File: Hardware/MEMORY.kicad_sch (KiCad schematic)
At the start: 11 parts, among them U20 AT24C256C

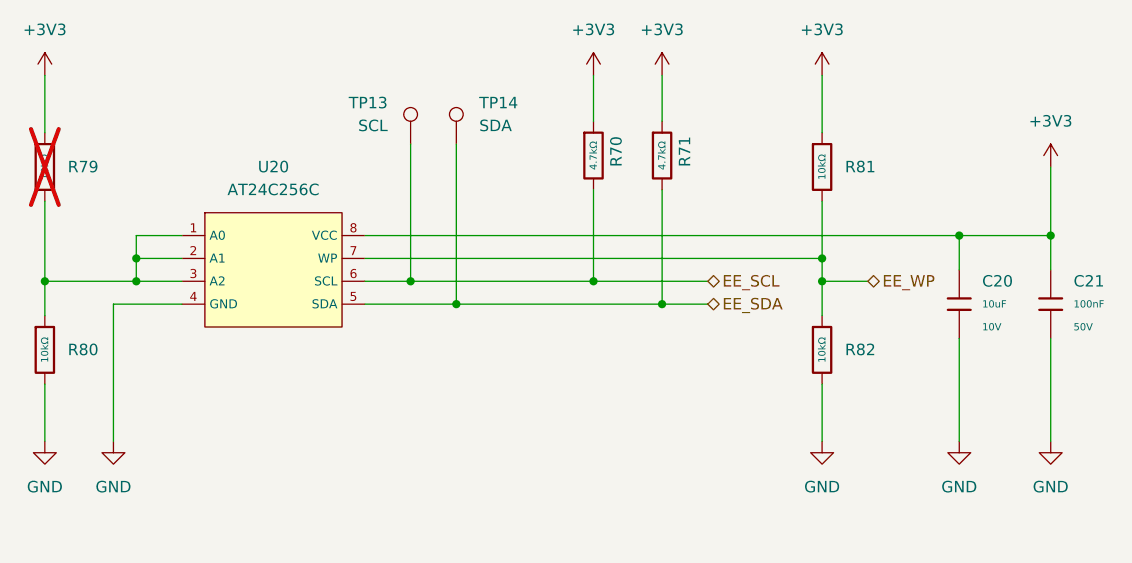
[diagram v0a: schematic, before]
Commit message: remove unused sheets
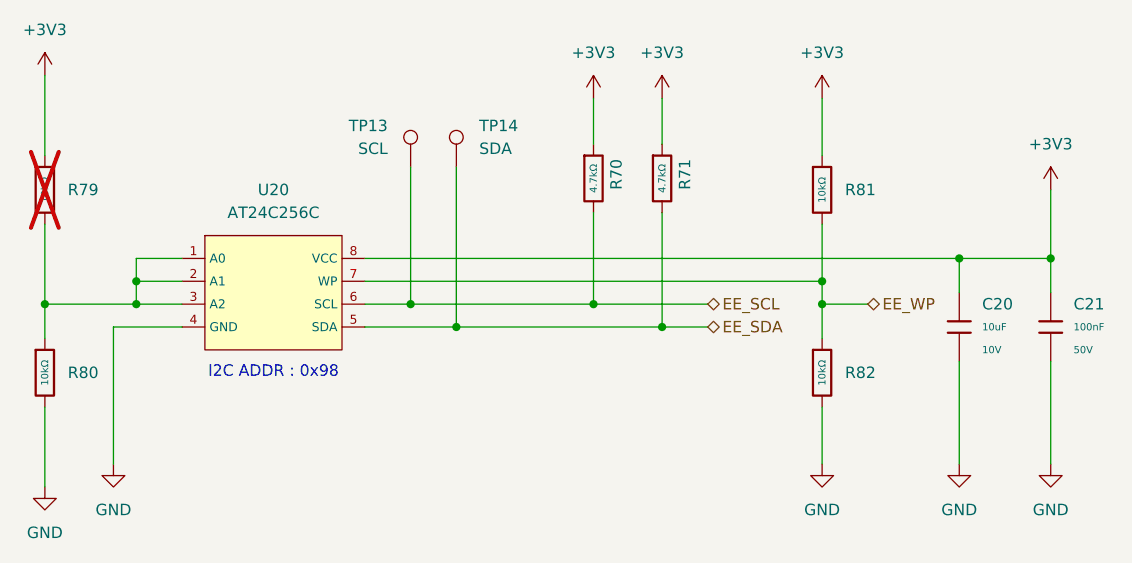
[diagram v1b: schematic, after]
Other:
- note added: "I2C ADDR : 0x98"
- moved on the sheet: C20, C21, R70, R71, R79, R80, R81, R82, TP13, TP14, U20
